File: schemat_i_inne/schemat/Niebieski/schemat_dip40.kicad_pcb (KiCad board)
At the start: 2 copper layers, 17 parts, among them J1 Conn_01x06_Female, SW1 Left, SW2 Up, SW3 Down, SW4 Right, SW5 Jump, SW6 Punch, SW7 SW_DIP_x01, U1 ATmega32A-AU, U2 WG12864B-STBL, U3 SD_card_reader, U4 L7805

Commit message: Schemat, scalenie i porzadki
->Zaktualizowano schemat
->Dodano skrypt manima.sh scalajacy poprzednie
->Dodano instrukcje tworzenia animacji
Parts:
- added Y1: 16Mhz, Crystal:Crystal_SMD_HC49-SD, F.Cu at (64.8, 81.4)
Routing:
- net Net-(U1-Pad8): track 0.00 -> 58.7 mm
- net Net-(U1-Pad7): track 0.00 -> 36.8 mm
- net GND: track 912.7 -> 923.1 mm
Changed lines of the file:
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@@
     (thickness 1.6)
     (drawings 0)
-    (tracks 265)
+    (tracks 278)
     (zones 0)
-    (modules 17)
+    (modules 18)
     (nets 45)
   )
@@
     (add_net VCC)
   )
+  (module Crystal:Crystal_SMD_HC49-SD (layer F.Cu)
+    (at 64.8462 81.3816)
+    (descr "SMD Crystal HC-49-SD http://cdn-reichelt.de/documents/datenblatt/B400/xxx-HC49-SMD.pdf, 11.4x4.7mm^2 package")
+    (tags "SMD SMT crystal")
+    (attr smd)
+    (fp_text reference Y1 (at 0 -3.55) (layer F.SilkS)
+      (effects (font (size 1 1) (thickness 0.15)))
+    )
+    (fp_text value 16Mhz (at 0 3.55) (layer F.Fab)
+      (effects (font (size 1 1) (thickness 0.15)))
+    )
+    (fp_arc (start 3.015 0) (end 3.015 -2.115) (angle 180) (layer F.Fab) (width 0.1))
+    (fp_arc (start -3.015 0) (end -3.015 -2.115) (angle -180) (layer F.Fab) (width 0.1))
+    (fp_line (start 6.8 -2.6) (end -6.8 -2.6) (layer F.CrtYd) (width 0.05))
+    (fp_line (start 6.8 2.6) (end 6.8 -2.6) (layer F.CrtYd) (width 0.05))
+    (fp_line (start -6.8 2.6) (end 6.8 2.6) (layer F.CrtYd) (width 0.05))
+    (fp_line (start -6.8 -2.6) (end -6.8 2.6) (layer F.CrtYd) (width 0.05))
+    (fp_line (start -6.7 2.55) (end 5.9 2.55) (layer F.SilkS) (width 0.12))
+    (fp_line (start -6.7 -2.55) (end -6.7 2.55) (layer F.SilkS) (width 0.12))
+    (fp_line (start 5.9 -2.55) (end -6.7 -2.55) (layer F.SilkS) (width 0.12))
+    (fp_line (start -3.015 2.115) (end 3.015 2.115) (layer F.Fab) (width 0.1))
+    (fp_line (start -3.015 -2.115) (end 3.015 -2.115) (layer F.Fab) (width 0.1))
+    (fp_line (start 5.7 -2.35) (end -5.7 -2.35) (layer F.Fab) (width 0.1))
+    (fp_line (start 5.7 2.35) (end 5.7 -2.35) (layer F.Fab) (width 0.1))
+    (fp_line (start -5.7 2.35) (end 5.7 2.35) (layer F.Fab) (width 0.1))
+    (fp_line (start -5.7 -2.35) (end -5.7 2.35) (layer F.Fab) (width 0.1))
+    (fp_text user %R (at 0 0) (layer F.Fab)
+      (effects (font (size 1 1) (thickness 0.15)))
+    )
+    (pad 2 smd rect (at 4.25 0) (size 4.5 2) (layers F.Cu F.Paste F.Mask)
+      (net 42 "Net-(U1-Pad7)"))
+    (pad 1 smd rect (at -4.25 0) (size 4.5 2) (layers F.Cu F.Paste F.Mask)
+      (net 41 "Net-(U1-Pad8)"))
+    (model ${KISYS3DMOD}/Crystal.3dshapes/Crystal_SMD_HC49-SD.wrl
+      (at (xyz 0 0 0))
+      (scale (xyz 1 1 1))
+      (rotate (xyz 0 0 0))
+    )
+  )
   (module Resistor_THT:R_Axial_DIN0309_L9.0mm_D3.2mm_P5.08mm_Vertical (layer F.Cu)
     (at 26.1747 49.7586 180)
@@
     )
   )
-  (segment (start 85.17 95.17) (end 70.92 95.17) (width 0.25) (layer F.Cu) (net 1))
-  (segment (start 101.379491 78.960509) (end 85.17 95.17) (width 0.25) (layer F.Cu) (net 1))
   (segment (start 70.92 95.17) (end 58.42 95.17) (width 0.25) (layer F.Cu) (net 1))
   (segment (start 53.14 74.755) (end 53.14 73.58) (width 0.25) (layer F.Cu) (net 1))
@@
   (segment (start 54.914 73.58) (end 53.14 73.58) (width 0.25) (layer F.Cu) (net 1))
   (segment (start 59.436 69.058) (end 54.914 73.58) (width 0.25) (layer F.Cu) (net 1))
-  (segment (start 59.436 64.516) (end 59.436 69.058) (width 0.25) (layer F.Cu) (net 1))
   (segment (start 236.524 74.85) (end 234.75 74.85) (width 0.25) (layer F.Cu) (net 1))
   (segment (start 248.92 62.454) (end 236.524 74.85) (width 0.25) (layer F.Cu) (net 1))
@@
   (segment (start 15.7099 54.8132) (end 15.748 55.88) (width 0.25) (layer F.Cu) (net 1))
   (segment (start 15.748 33.528) (end 15.7099 54.8132) (width 0.25) (layer F.Cu) (net 1))
+  (segment (start 101.379491 78.960509) (end 99.568 80.772) (width 0.25) (layer F.Cu) (net 1))
+  (segment (start 99.568 80.772) (end 76.3397 80.772) (width 0.25) (layer F.Cu) (net 1))
+  (segment (start 64.4525 68.8848) (end 59.436 68.8848) (width 0.25) (layer F.Cu) (net 1))
+  (segment (start 76.3397 80.772) (end 64.4525 68.8848) (width 0.25) (layer F.Cu) (net 1))
+  (segment (start 59.436 68.8848) (end 59.436 69.058) (width 0.25) (layer F.Cu) (net 1))
+  (segment (start 59.436 64.516) (end 59.436 68.8848) (width 0.25) (layer F.Cu) (net 1))
   (segment (start 247.82 24.13) (end 248.92 24.13) (width 0.25) (layer F.Cu) (net 2))
   (segment (start 226.738 24.13) (end 247.82 24.13) (width 0.25) (layer F.Cu) (net 2))
@@
   (segment (start 123.698001 51.561999) (end 123.698001 67.496131) (width 0.25) (layer F.Cu) (net 38))
   (segment (start 124.46 50.8) (end 123.698001 51.561999) (width 0.25) (layer F.Cu) (net 38))
+  (segment (start 58.0962 81.3816) (end 55.9435 83.5343) (width 0.25) (layer F.Cu) (net 41))
+  (segment (start 60.5962 81.3816) (end 58.0962 81.3816) (width 0.25) (layer F.Cu) (net 41))
+  (segment (start 55.9435 83.5343) (end 55.9435 86.0425) (width 0.25) (layer F.Cu) (net 41))
+  (segment (start 55.9435 86.0425) (end 57.912 88.011) (width 0.25) (layer F.Cu) (net 41))
+  (segment (start 94.591742 88.011) (end 102.510862 80.09188) (width 0.25) (layer F.Cu) (net 41))
+  (segment (start 57.912 88.011) (end 94.591742 88.011) (width 0.25) (layer F.Cu) (net 41))
+  (segment (start 69.0962 82.6316) (end 70.7799 84.3153) (width 0.25) (layer F.Cu) (net 42))
+  (segment (start 69.0962 81.3816) (end 69.0962 82.6316) (width 0.25) (layer F.Cu) (net 42))
+  (segment (start 97.156071 84.3153) (end 101.945177 79.526194) (width 0.25) (layer F.Cu) (net 42))
+  (segment (start 70.7799 84.3153) (end 97.156071 84.3153) (width 0.25) (layer F.Cu) (net 42))
   (segment (start 33.6713 42.262) (end 34.456 42.262) (width 0.25) (layer F.Cu) (net 44))
   (segment (start 26.1747 49.7586) (end 33.6713 42.262) (width 0.25) (layer F.Cu) (net 44))

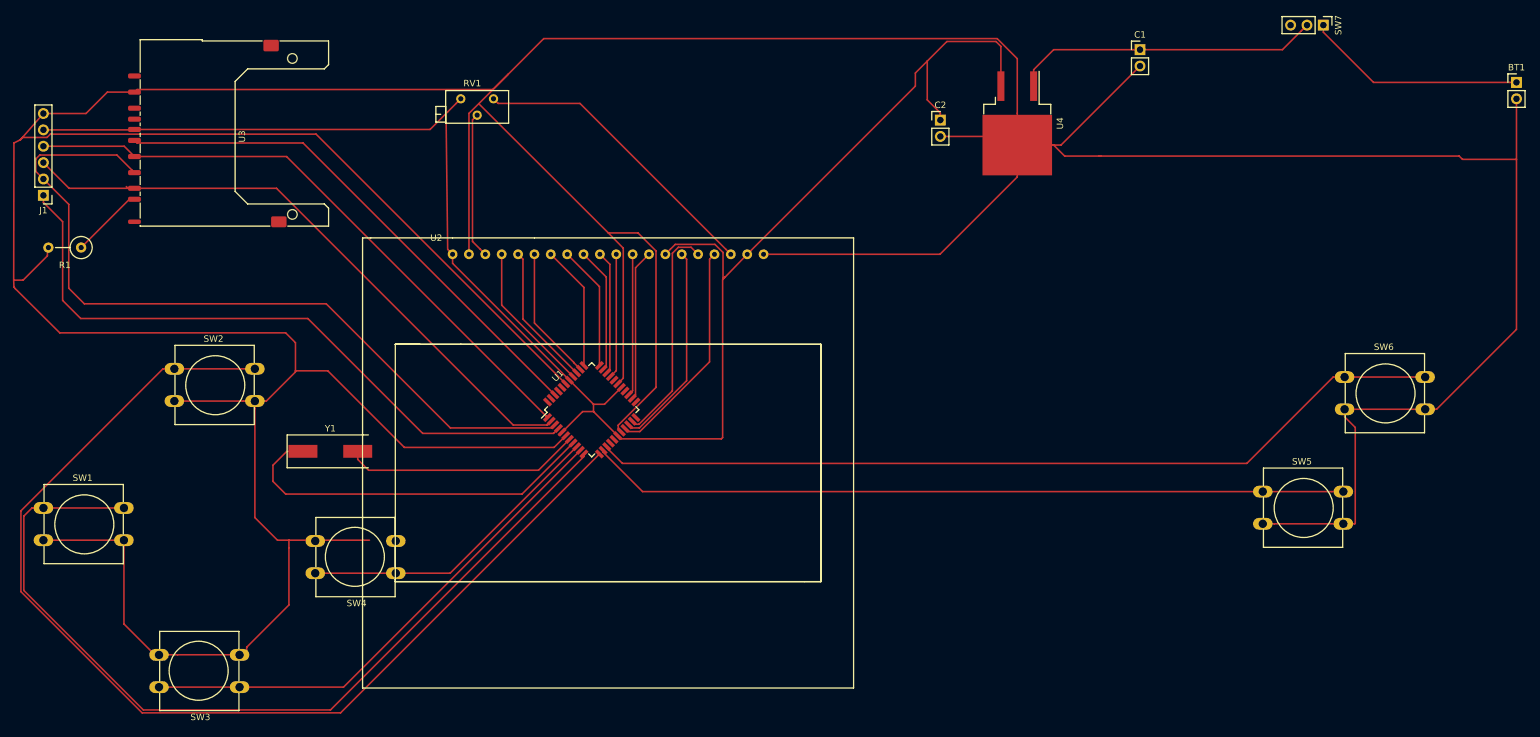
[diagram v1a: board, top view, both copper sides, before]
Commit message: Zmieniono uklad symboli na plytce
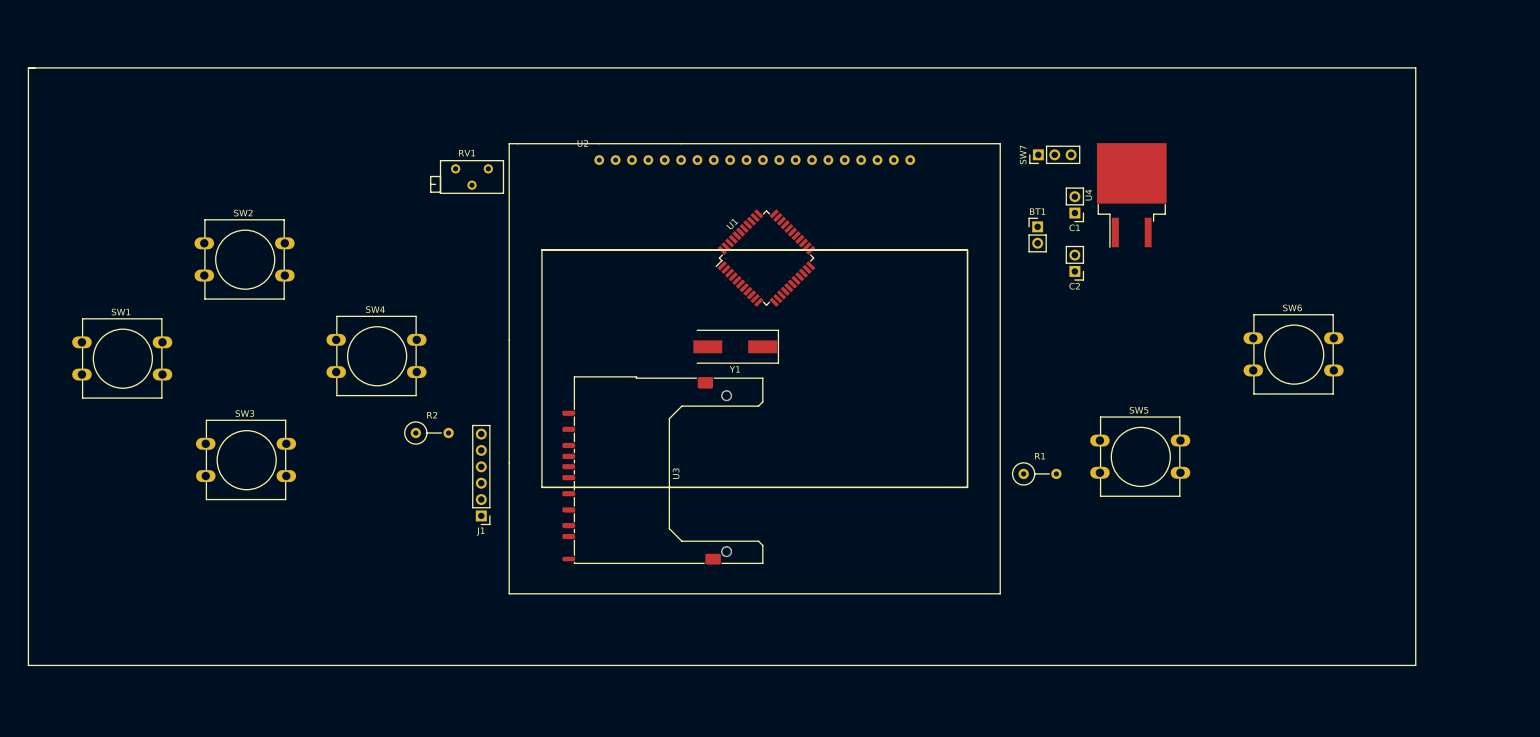
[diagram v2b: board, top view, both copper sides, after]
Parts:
- added R2: 0R, Resistor_THT:R_Axial_DIN0309_L9.0mm_D3.2mm_P5.08mm_Vertical, F.Cu at (78.1, 78.5)
- moved R1 150.4 mm to (172.4, 84.9), turned to 0 degrees
- moved U3 85.3 mm to (109.0, 84.8)
- moved J1 84.2 mm to (88.3, 91.4)
- moved BT1 77.6 mm to (174.6, 46.5)
- moved Y1 64.9 mm to (127.7, 65.2), turned to 180 degrees
- moved SW7 48.6 mm to (174.7, 35.4), turned to 90 degrees
- moved SW3 38.1 mm to (45.5, 80.2), turned to 0 degrees
- moved SW4 37.4 mm to (65.8, 64.1), turned to 0 degrees
- moved U1 35.9 mm to (132.5, 51.4)
- moved C2 31.4 mm to (180.4, 53.5), turned to 180 degrees
- moved C1 27.3 mm to (180.4, 44.4), turned to 180 degrees
- moved U2 27.1 mm to (115.5, 47.6)
- moved SW5 26.5 mm to (184.3, 79.7)
- moved SW1 26.4 mm to (26.3, 64.5)
- moved U4 21.0 mm to (189.2, 41.6), turned to 90 degrees
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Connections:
- SW3 pad 2: GND -> Net-(R2-Pad1)
- SW4 pad 2: GND -> Net-(R2-Pad1)
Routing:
- net GND: track 923.1 -> 0.00 mm
- net VCC: track 271.8 -> 0.00 mm
- net Net-(SW2-Pad1): track 172.2 -> 0.00 mm
- net Net-(SW1-Pad1): track 138.9 -> 0.00 mm
- net Net-(SW6-Pad1): track 133.7 -> 0.00 mm
- net Net-(J1-Pad2): track 123.5 -> 0.00 mm
- net Net-(SW5-Pad1): track 117.7 -> 0.00 mm
- net Net-(J1-Pad1): track 103.4 -> 0.00 mm
- net Net-(J1-Pad3): track 97.3 -> 0.00 mm
- net Net-(J1-Pad4): track 95.7 -> 0.00 mm
- net Net-(U1-Pad42): track 81.6 -> 0.00 mm
- net Net-(SW3-Pad1): track 80.6 -> 0.00 mm
- net Net-(U1-Pad8): track 58.7 -> 0.00 mm
- net Net-(SW4-Pad1): track 48.7 -> 0.00 mm
- net Net-(C1-Pad1): track 47.8 -> 0.00 mm
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
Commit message: Dodane polaczenia
Dodano wszystkie polaczenia
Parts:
- removed R1, R2: 0R, Resistor_THT:R_Axial_DIN0309_L9.0mm_D3.2mm_P5.08mm_Vertical
- moved U1 34.7 mm to (127.5, 85.7)
- moved J1 34.0 mm to (84.3, 57.6)
- moved Y1 33.7 mm to (111.1, 94.5)
- moved U4 30.5 mm to (109.3, 54.3)
- moved U3 4.28 mm to (116.7, 43.5)
- renumbered SW7 to SW1, SW1 to SW2, SW2 to SW3, SW3 to SW4, SW4 to SW5, SW5 to SW6, SW6 to SW7, U4 to U2, U2 to U3, U3 to U4
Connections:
- SW4 pad 2: Net-(R2-Pad1) -> GND
- SW5 pad 2: Net-(R2-Pad1) -> GND
- U4 pad 8: Net-(R1-Pad1) -> GND
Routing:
- net GND: track 0.00 -> 577.8 mm
- net VCC: track 0.00 -> 334.7 mm
- net Net-(SW3-Pad1): track 0.00 -> 164.4 mm
- net Net-(SW2-Pad1): track 0.00 -> 133.5 mm
- net Net-(SW7-Pad1): track 0.00 -> 103.1 mm
- net Net-(SW4-Pad1): track 0.00 -> 88.6 mm
- net Net-(SW5-Pad1): track 0.00 -> 78.7 mm
- net Net-(SW6-Pad1): track 0.00 -> 73.2 mm
- net Net-(RV1-Pad1): track 0.00 -> 65.5 mm
- net Net-(U1-Pad19): track 0.00 -> 65.3 mm
- net Net-(U1-Pad21): track 0.00 -> 61.9 mm
- net Net-(J1-Pad3): track 0.00 -> 61.2 mm
- net Net-(U1-Pad20): track 0.00 -> 60.8 mm
- net Net-(J1-Pad2): track 0.00 -> 58.8 mm
- net Net-(J1-Pad4): track 0.00 -> 58.4 mm
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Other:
- board outline added: 203.2 x 73.7 mm

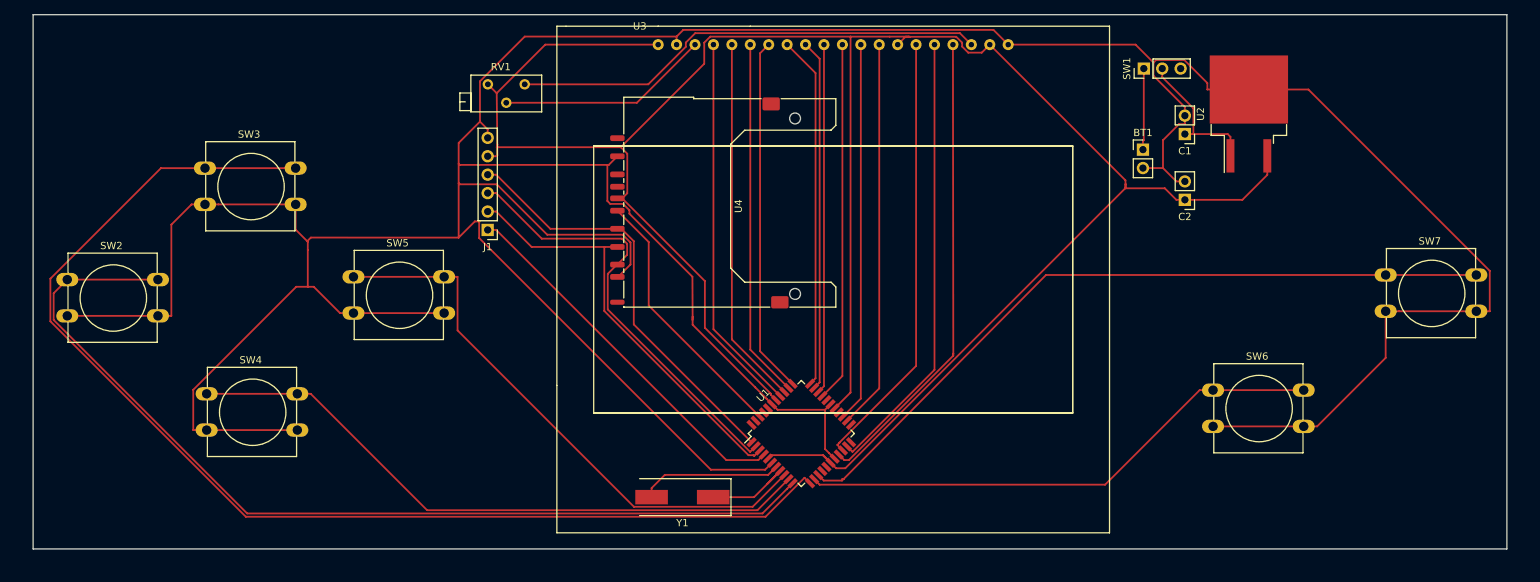
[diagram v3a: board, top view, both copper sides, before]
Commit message: Lepsze sciezki, wypelnione GND
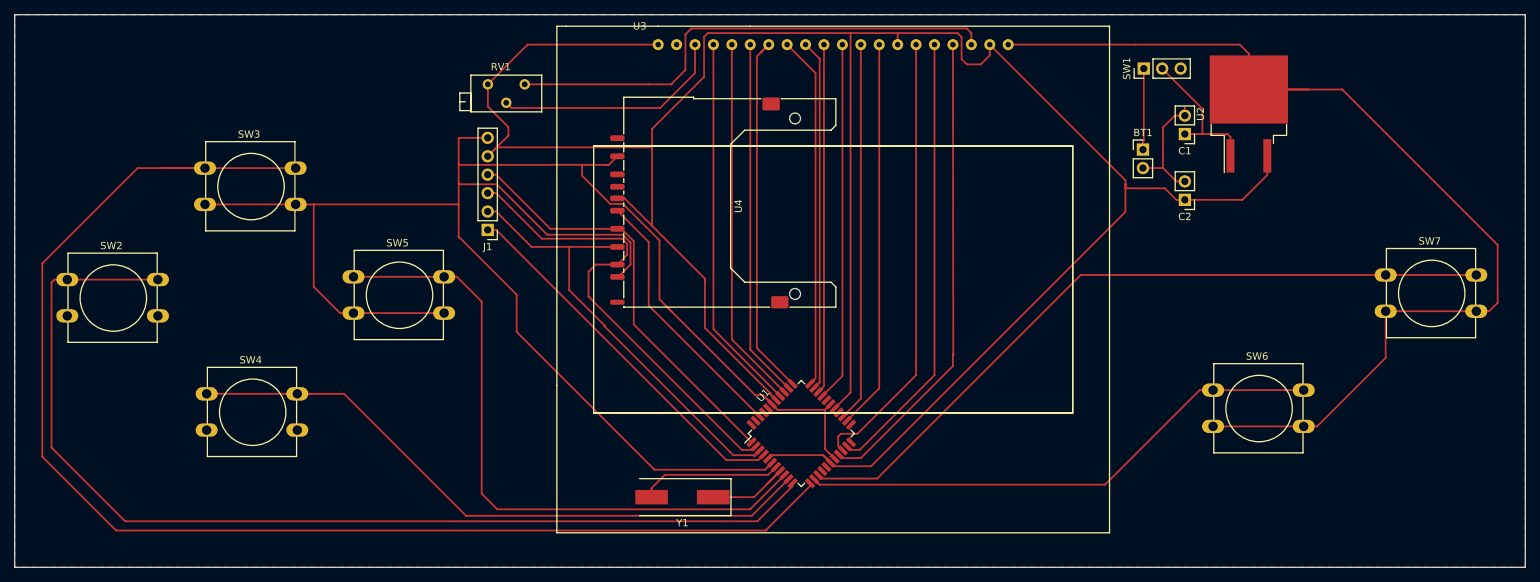
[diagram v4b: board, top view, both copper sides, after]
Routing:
- net GND: track 577.8 -> 428.1 mm
- net Net-(SW3-Pad1): track 164.4 -> 186.1 mm
- net VCC: track 334.7 -> 350.2 mm
- net Net-(SW2-Pad1): track 133.5 -> 146.4 mm
- net Net-(SW5-Pad1): track 78.7 -> 90.2 mm
- net Net-(J1-Pad3): track 61.2 -> 65.4 mm
- net Net-(RV1-Pad1): track 65.5 -> 69.6 mm
- net Net-(J1-Pad2): track 58.8 -> 62.0 mm
- net Net-(RV1-Pad2): track 29.3 -> 32.2 mm
- net Net-(SW4-Pad1): track 88.6 -> 91.1 mm
- net Net-(U1-Pad34): track 49.1 -> 51.2 mm
- net Net-(U1-Pad20): track 60.8 -> 62.1 mm
- net Net-(SW7-Pad1): track 103.1 -> 102.6 mm
- net Net-(C1-Pad1): track 19.9 -> 20.4 mm
- net Net-(U1-Pad19): track 65.3 -> 65.8 mm
- added copper zone on F.Cu, net GND
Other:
- board size 203.2 x 73.7 mm -> 208.3 x 76.2 mm

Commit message: Buzzer
Dodano buzzer
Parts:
- added BZ1: Buzzer, Buzzer_Beeper:Buzzer_12x9.5RM7.6, F.Cu at (208.0, 38.2)
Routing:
- net Net-(BZ1-Pad1): track 0.00 -> 99.2 mm
- net GND: track 428.1 -> 367.1 mm
